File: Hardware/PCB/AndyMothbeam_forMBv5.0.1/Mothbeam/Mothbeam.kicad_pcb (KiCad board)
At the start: 2 copper layers, 26.8 x 45 mm, 23 parts, among them CN1 X6511FRS-04-C85D30, SW2 SW_DIP_x04, U1 BCR421U, U2 BCR421U, U3 BCR421U

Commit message: Mothbeam +-
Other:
- board text added: "+"
- board text added: "-"
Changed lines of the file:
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@@
+		)
+	)
+	(gr_text "-"
+		(at 109.45 56.65 0)
+		(layer "F.SilkS")
+		(effects
+			(font
+				(size 1 1)
+				(thickness 0.1)
+			)
+			(justify left bottom)
 		)
 	)
@@
 			)
 			(justify right bottom)
+		)
+	)
+	(gr_text "-"
+		(at 109.3 41.05 0)
+		(layer "F.SilkS")
+		(effects
+			(font
+				(size 1 1)
+				(thickness 0.1)
+			)
+			(justify left bottom)
 		)
 	)
@@
 		)
 	)
+	(gr_text "-"
+		(at 109.5 48.8 0)
+		(layer "F.SilkS")
+		(effects
+			(font
+				(size 1 1)
+				(thickness 0.1)
+			)
+			(justify left bottom)
+		)
+	)
 	(gr_text "+70mA"
 		(at 109.576407 73.878474 0)
@@
 			)
 			(justify right bottom)
+		)
+	)
+	(gr_text "+"
+		(at 109.45 52.05 0)
+		(layer "F.SilkS")
+		(effects
+			(font
+				(size 1 1)
+				(thickness 0.1)
+			)
+			(justify left bottom)
 		)
 	)
@@
 			)
 			(justify left bottom)
+		)
+	)
+	(gr_text "+"
+		(at 109.3 36.45 0)
+		(layer "F.SilkS")
+		(effects
+			(font
+				(size 1 1)
+				(thickness 0.1)
+			)
+			(justify left bottom)
+		)
+	)
+	(gr_text "+"
+		(at 109.5 44.2 0)
+		(layer "F.SilkS")
+		(effects
+			(font
+				(size 1 1)
+				(thickness 0.1)
+			)
+			(justify left bottom)

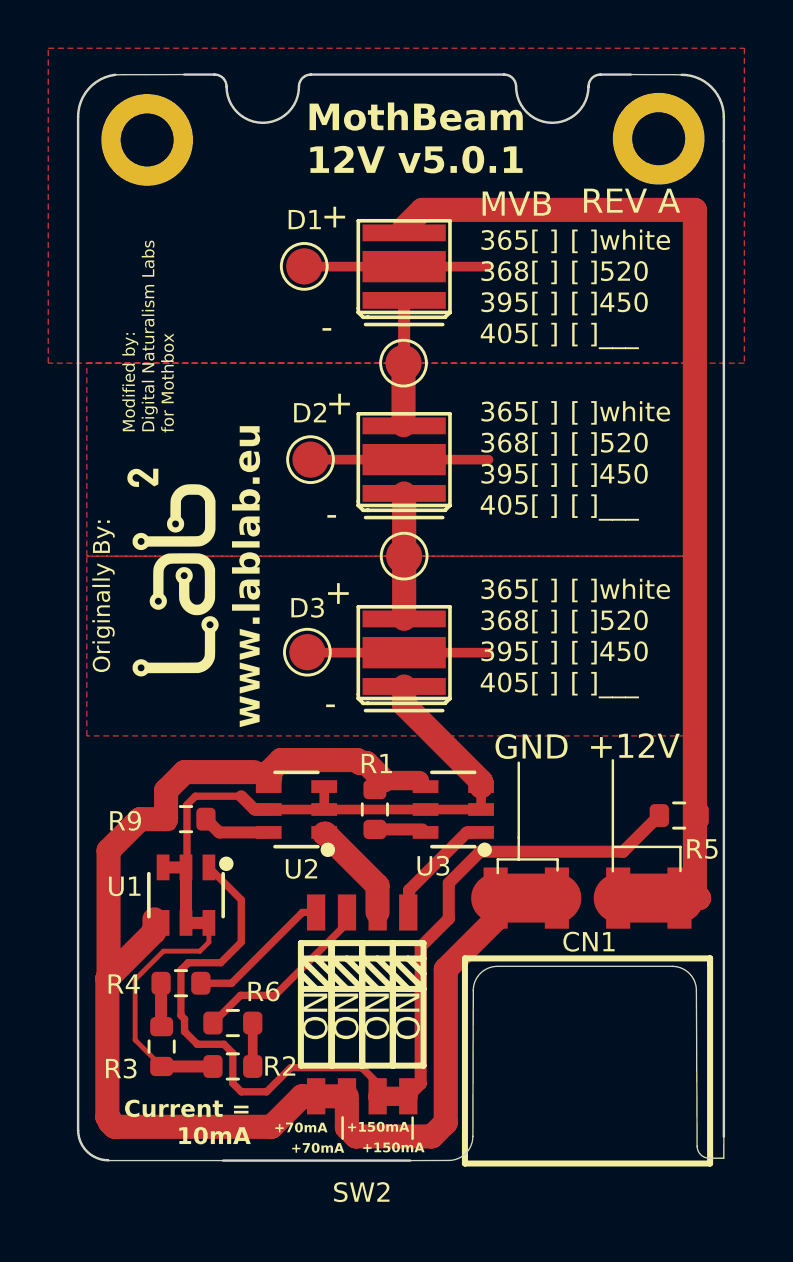
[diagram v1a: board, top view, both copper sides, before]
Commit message: updated MothBeam PCB Edge and MothBox PCB
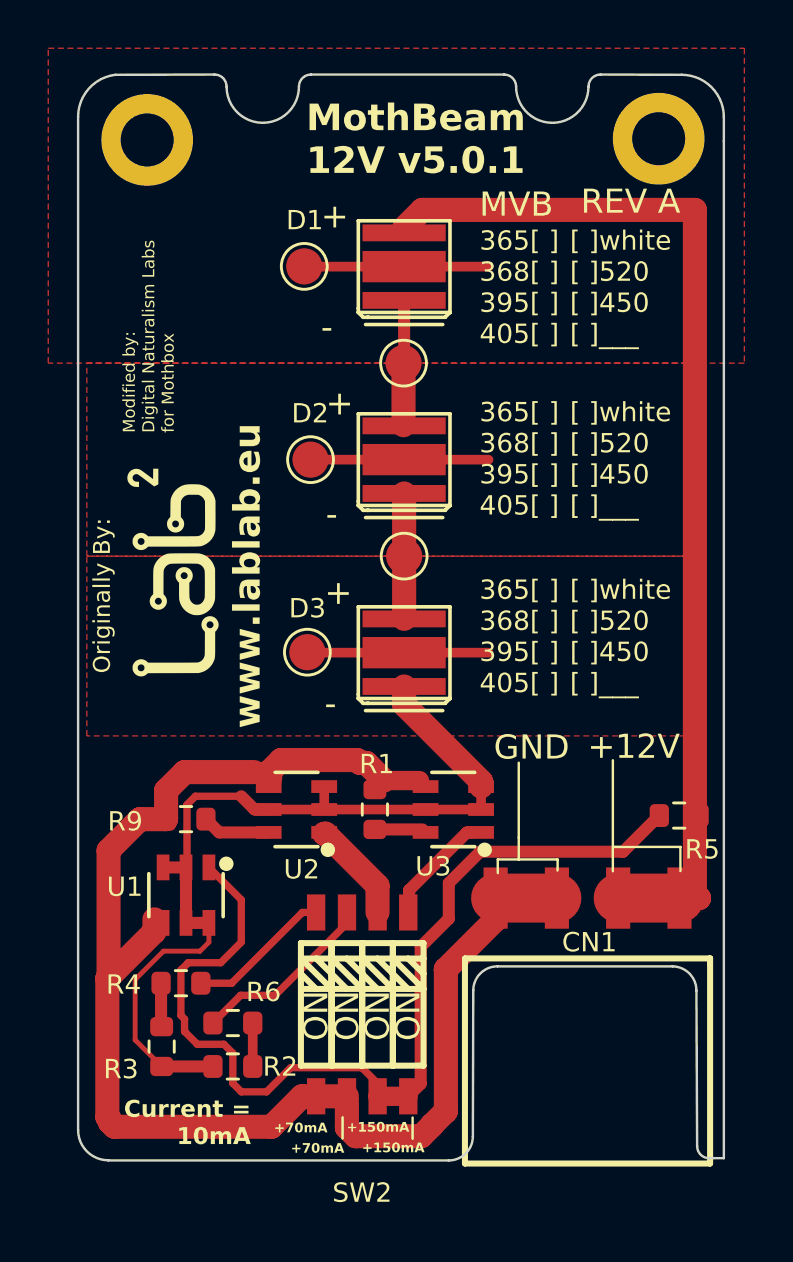
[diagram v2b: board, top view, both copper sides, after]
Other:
- outline, holes or cut-outs redrawn
